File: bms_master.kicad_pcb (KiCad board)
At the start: 4 copper layers, 100 x 50 mm, 25 parts, among them J1 0430450200, J3 TFM-115-02-S-D-WT, J4 0436500200, J4 TFM-115-02-S-D-WT, U2 SM91502ALA-E, U3 SM91502ALA-E

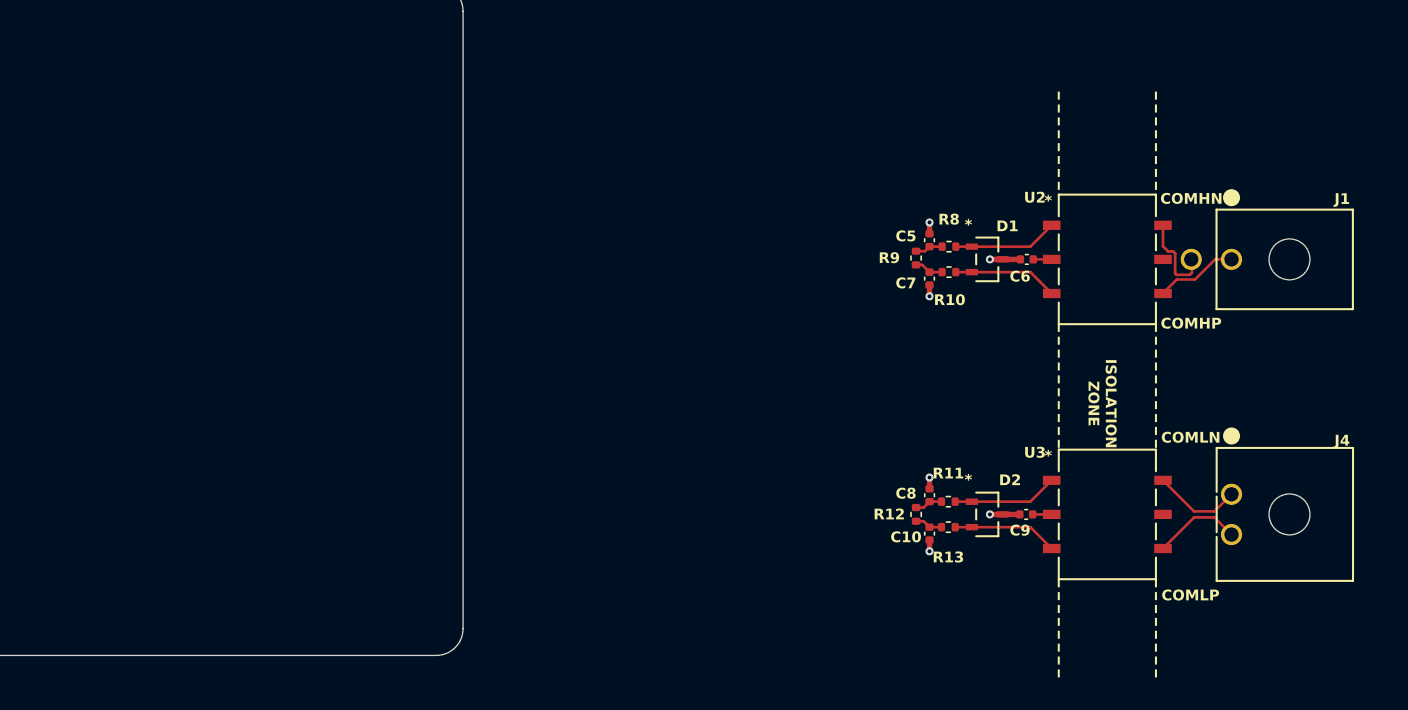
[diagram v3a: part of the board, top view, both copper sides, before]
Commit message: PCB[Fixed Lib Link]: Placed iso parts need to fix arrangment.
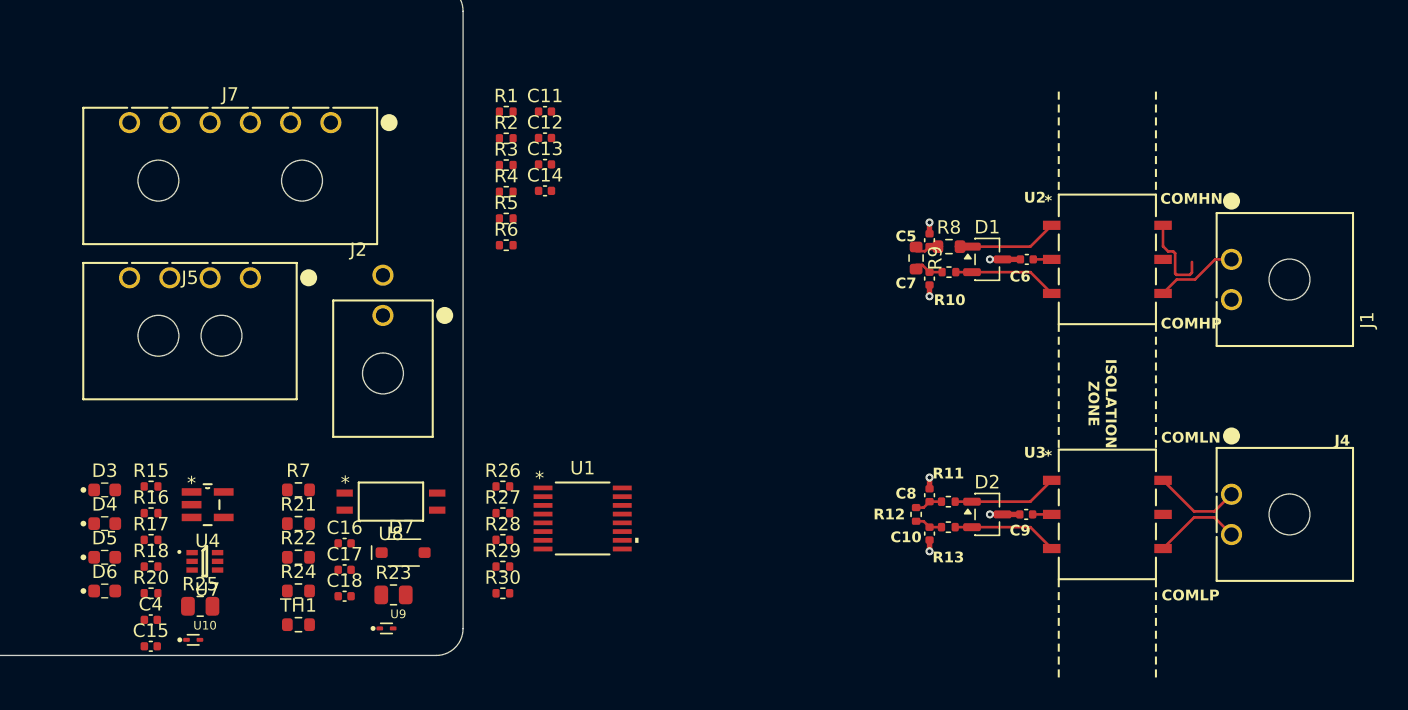
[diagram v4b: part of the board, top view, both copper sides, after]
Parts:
- added C11: 100 pF, remote_cl05a105ko5nnnc:C_0402_1005Metric, F.Cu at (170.1, 65.5)
- added C12: 100 pF, remote_cl05a105ko5nnnc:C_0402_1005Metric, F.Cu at (170.1, 67.5)
- added C13: 100 pF, remote_cl05a105ko5nnnc:C_0402_1005Metric, F.Cu at (170.1, 69.4)
- added C14: 100 pF, remote_cl05a105ko5nnnc:C_0402_1005Metric, F.Cu at (170.1, 71.4)
- added C15: 0.1 µF, remote_cl05a105ko5nnnc:C_0402_1005Metric, F.Cu at (140.7, 105.3)
- added C16: 0.1 µF, remote_cl05a105ko5nnnc:C_0402_1005Metric, F.Cu at (155.2, 97.7)
- added C17: 10 nF, remote_cl05a105ko5nnnc:C_0402_1005Metric, F.Cu at (155.2, 99.6)
- added C18: 10 nF, remote_cl05a105ko5nnnc:C_0402_1005Metric, F.Cu at (155.2, 101.6)
- added C4: 0.1 µF, remote_cl05a105ko5nnnc:C_0402_1005Metric, F.Cu at (140.7, 103.4)
- added D3: Green, remote_ltst-c190tbkt:LED_0603_1608Metric, F.Cu at (137.3, 93.7)
- added D4: Green, remote_ltst-c190tbkt:LED_0603_1608Metric, F.Cu at (137.3, 96.2)
- added D5: RED, remote_ltst-c190tbkt:LED_0603_1608Metric, F.Cu at (137.3, 98.7)
- added D6: RED, remote_ltst-c190tbkt:LED_0603_1608Metric, F.Cu at (137.3, 101.2)
- added D7: 1N4148W, remote_1n4148w:P35_SOD-123F, F.Cu at (157.9, 98.3)
- added J2: 0430450200, remote_0430450200:CONN_SD-43045-001_02_MOL, F.Cu at (158.0, 80.7)
- added J5: 0436500400, remote_0436500400:CONN_SD-43650-001_04_MOL, F.Cu at (148.2, 77.9)
- added J7: 0436500600, remote_0436500600:CONN_SD-43650-001_06_MOL, F.Cu at (154.2, 66.3)
- added R1: 1k, remote_erj-2ge0r00x:R_0402_1005Metric, F.Cu at (167.2, 65.5)
- added R15: 10k, remote_erj-2ge0r00x:R_0402_1005Metric, F.Cu at (140.8, 93.4)
- added R16: 10k, remote_erj-2ge0r00x:R_0402_1005Metric, F.Cu at (140.8, 95.4)
- added R17: 10k, remote_erj-2ge0r00x:R_0402_1005Metric, F.Cu at (140.8, 97.4)
- added R18: 1k, remote_erj-2ge0r00x:R_0402_1005Metric, F.Cu at (140.8, 99.4)
- added R2: 1k, remote_erj-2ge0r00x:R_0402_1005Metric, F.Cu at (167.2, 67.5)
- added R20: 1k, remote_erj-2ge0r00x:R_0402_1005Metric, F.Cu at (140.8, 101.4)
- added R21: 10k, remote_rcs060359r0fkea:R_0603_1608Metric, F.Cu at (151.7, 96.2)
- added R22: 10k, remote_rcs060359r0fkea:R_0603_1608Metric, F.Cu at (151.7, 98.7)
- added R23: 10k, remote_crcw080510k0fkea:R_0805_2012Metric, F.Cu at (158.8, 101.5)
- added R24: 22k, remote_rcs060359r0fkea:R_0603_1608Metric, F.Cu at (151.7, 101.2)
- added R25: 330, remote_crcw080510k0fkea:R_0805_2012Metric, F.Cu at (144.4, 102.3)
- added R26: 10k, remote_erj-2ge0r00x:R_0402_1005Metric, F.Cu at (167.0, 93.4)
- added R27: 10k, remote_erj-2ge0r00x:R_0402_1005Metric, F.Cu at (167.0, 95.4)
- added R28: 10k, remote_erj-2ge0r00x:R_0402_1005Metric, F.Cu at (167.0, 97.4)
- added R29: 10k, remote_erj-2ge0r00x:R_0402_1005Metric, F.Cu at (167.0, 99.4)
- added R3: 49.9, remote_erj-2ge0r00x:R_0402_1005Metric, F.Cu at (167.2, 69.5)
- added R30: 10k, remote_erj-2ge0r00x:R_0402_1005Metric, F.Cu at (167.0, 101.4)
- added R4: 49.9, remote_erj-2ge0r00x:R_0402_1005Metric, F.Cu at (167.2, 71.5)
- added R5: 49.9, remote_erj-2ge0r00x:R_0402_1005Metric, F.Cu at (167.2, 73.5)
- added R6: 49.9, remote_erj-2ge0r00x:R_0402_1005Metric, F.Cu at (167.2, 75.4)
- added R7: 10k, remote_rcs060359r0fkea:R_0603_1608Metric, F.Cu at (151.7, 93.7)
- added TH1: NCP18XH103F03RB, remote_rcs060359r0fkea:R_0603_1608Metric, F.Cu at (151.7, 103.7)
- added U1: BQ79600PWRQ1, remote_bq79600pwrq1:SOIC_9600PWQ1_TEX, F.Cu at (172.9, 95.8)
- added U10: ESD9B5.0ST5G, remote_esd9b3.3st5g:SODFL1006X40N, F.Cu at (143.9, 104.8)
- added U4: SN74LVC1G08QDBVRQ1, remote_sn74lvc1g08qdbvrq1:DBV5, F.Cu at (145.0, 94.8)
- added U7: SN74LVC2G04DCKR, remote_sn74lvc2g04dckr:DCK0006A_N, F.Cu at (144.8, 99.0)
- added U8: TLP293(GB-TPL,E, remote_tlp293_gb-tpl_e:SO4_TOS, F.Cu at (158.6, 94.5)
- added U9: ESD9B5.0ST5G, remote_esd9b3.3st5g:SODFL1006X40N, F.Cu at (158.3, 104.0)
- C10, C8: value 100 pF -> 0.1 µF
- C5: value 100 pF -> 100pF
- C7: value 100 pF -> 220 nF
- C9: value 100pF -> 220 nF
- D1, D2: footprint remote_pesd1can_215:SOT23_PESD1_NEX -> remote_pesd5v0u2bt-qr:SOT-23-3
- J1: value 0430450200 -> 0436500200; footprint remote_0430450200:CONN_SD-43045-001_02_MOL -> remote_0436500200:CONN_SD-43650-001_02_MOL
- R10, R11: value 49.9 -> 1k
- R8: value 49.9 -> 10; footprint remote_erj-2ge0r00x:R_0402_1005Metric -> remote_rcs060359r0fkea:R_0603_1608Metric
- R9: value 1k -> 100k; footprint remote_erj-2ge0r00x:R_0402_1005Metric -> remote_rcs060359r0fkea:R_0603_1608Metric
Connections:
- C10 pad 1: /Project Architecture/GND -> /Project Architecture/Com. Chip/BAT
- C10 pad 2: /Project Architecture/Com. Chip/U1_COML.P -> /Project Architecture/GND
- C5 pad 1: /Project Architecture/GND -> /Project Architecture/Daisy Chain/COMH_CT
- C5 pad 2: /Project Architecture/Com. Chip/U1_COMH.P -> /Project Architecture/GND
- C6 pad 1: /Project Architecture/Daisy Chain/COMH_CT -> /Project Architecture/Daisy Chain/COML_CT
- C7 pad 2: /Project Architecture/Com. Chip/U1_COMH.N -> /Project Architecture/Com. Chip/DVDD
- C8 pad 1: /Project Architecture/GND -> /Project Architecture/+3V3
- C8 pad 2: /Project Architecture/Com. Chip/U1_COML.N -> /Project Architecture/GND
- C9 pad 1: /Project Architecture/Daisy Chain/COML_CT -> /Project Architecture/Com. Chip/CVDD
- J1 pad 1: /Project Architecture/Connectors/COMH.N -> /Project Architecture/Connectors/COML.N
- J1 pad 2: /Project Architecture/Connectors/COMH.P -> /Project Architecture/Connectors/COML.P
- J3 pad 01: /Project Architecture/Connectors/BOARD_TEMP -> /Project Architecture/+12V
- J3 pad 02: /Project Architecture/Connectors/BOARD_TEMP -> /Project Architecture/+12V
- J3 pad 03: /Project Architecture/GND -> /Project Architecture/+5V
- J3 pad 04: /Project Architecture/GND -> /Project Architecture/+5V
- J3 pad 05: unconnected-(J3-ADC1_IN2-Pad05) -> /Project Architecture/+3V3
- J3 pad 06: unconnected-(J3-ADC1_IN2-Pad06) -> /Project Architecture/+3V3
- J3 pad 11: /Project Architecture/GND -> unconnected-(J3-TIM1_CH3-Pad11)
- J3 pad 12: /Project Architecture/GND -> unconnected-(J3-TIM2_CH1-Pad12)
- J3 pad 14: unconnected-(J3-ADC1_IN4-Pad14) -> /Project Architecture/Com. Chip/SPI.nCS
- J3 pad 15: /Project Architecture/GND -> /Project Architecture/Com. Chip/SPI.RDY
- J3 pad 16: /Project Architecture/GND -> /Project Architecture/BMS_OK & Indicators/FB.NFAULT
- J3 pad 17: unconnected-(J3-ADC2_IN5-Pad17) -> /Project Architecture/Connectors/MCU_BMS_OK
- J3 pad 18: unconnected-(J3-ADC2_IN5-Pad18) -> /Project Architecture/Connectors/CHG_MODE_N
- J3 pad 19: /Project Architecture/GND -> /Project Architecture/BMS_OK & Indicators/FB.BMS_OK
- J3 pad 20: /Project Architecture/GND -> /Project Architecture/Connectors/SDC_OK_N
- J3 pad 21: unconnected-(J3-DAC1_OUT2-Pad21) -> /Project Architecture/Com. Chip/SPI.MOSI
- J3 pad 22: unconnected-(J3-DAC1_OUT2-Pad22) -> /Project Architecture/Com. Chip/SPI.MISO
- J3 pad 25: unconnected-(J3-DAC1_OUT1-Pad25) -> /Project Architecture/GND
- J3 pad 26: unconnected-(J3-DAC1_OUT1-Pad26) -> /Project Architecture/Com. Chip/SPI.SCLK
- J3 pad 29: /Project Architecture/GND -> unconnected-(J3-I2C1_SCL-Pad29)
- J3 pad 30: /Project Architecture/GND -> unconnected-(J3-I2C1_SDA-Pad30)
- R10 pad 1: /Project Architecture/Com. Chip/U1_COMH.N -> Net-(D3-A)
- R10 pad 2: /Project Architecture/Daisy Chain/COMH_WN -> /Project Architecture/+3V3
- R11 pad 1: /Project Architecture/Com. Chip/U1_COML.N -> Net-(D4-A)
- R11 pad 2: /Project Architecture/Daisy Chain/COML_WN -> /Project Architecture/BMS_OK & Indicators/BMS_OK_LOGIC
- R8 pad 1: /Project Architecture/Com. Chip/U1_COMH.P -> /Project Architecture/Com. Chip/BAT
- R8 pad 2: /Project Architecture/Daisy Chain/COMH_WP -> /Project Architecture/+12V
- R9 pad 1: /Project Architecture/Com. Chip/U1_COMH.P -> /Project Architecture/BMS_OK & Indicators/NFAULT
- R9 pad 2: /Project Architecture/Com. Chip/U1_COMH.N -> /Project Architecture/+3V3
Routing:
- net (no net): track 8.39 -> 0.00 mm
- net /Project Architecture/GND: track 4.49 -> 9.18 mm, vias 2 -> 5
- net /Project Architecture/Daisy Chain/COMH_CT: track 1.37 -> 3.45 mm
- net /Project Architecture/Com. Chip/U1_COML.P: track 0.84 -> 2.07 mm, vias 1 -> 0
- net /Project Architecture/Com. Chip/U1_COML.N: track 0.84 -> 2.07 mm, vias 1 -> 0
- net /Project Architecture/Com. Chip/U1_COMH.P: track 0.84 -> 0.00 mm, vias 1 -> 0
- net /Project Architecture/Com. Chip/U1_COMH.N: track 0.84 -> 0.00 mm, vias 1 -> 0
- net /Project Architecture/Com. Chip/DVDD: track 0.00 -> 0.84 mm, vias 0 -> 1

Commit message: PCB[Layout, Mounting]:Inital layout and edgecut/hole placment.
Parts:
- removed C16: 0.1 µF, remote_cl05a105ko5nnnc:C_0402_1005Metric
- removed C17, C18: 10 nF, remote_cl05a105ko5nnnc:C_0402_1005Metric
- removed the J4 at (221.2, 94.0)
- removed J7: 0436500600, remote_0436500600:CONN_SD-43650-001_06_MOL
- removed R27, R28, R29, R30: 10k, remote_erj-2ge0r00x:R_0402_1005Metric
- removed U10, U9: ESD9B5.0ST5G, remote_esd9b3.3st5g:SODFL1006X40N
- added C1: 220 nF, remote_cl05a105ko5nnnc:C_0402_1005Metric, F.Cu at (111.5, 77.6)
- added C2: 0.1 µF, remote_cl05a105ko5nnnc:C_0402_1005Metric, F.Cu at (116.6, 77.6)
- added C3: 0.1 µF, remote_cl05a105ko5nnnc:C_0402_1005Metric, F.Cu at (108.4, 79.6)
- added G1: SAE Electric logo, remote_sae_electric_logo:SAE_Electric_Logo_10mm, F.Cu at (73.2, 64.8)
- added G2: BMD Logo, remote_bmd_logo:BDM_Logo_100mm, B.Cu at (116.2, 82.0)
- added R14: 1k, remote_erj-2ge0r00x:R_0402_1005Metric, F.Cu at (79.7, 100.6)
- added R19: 10k, remote_erj-2ge0r00x:R_0402_1005Metric, F.Cu at (105.8, 77.7)
- added U5: ESD9B5.0ST5G, remote_esd9b3.3st5g:SODFL1006X40N, F.Cu at (75.8, 88.0)
- added U6: SN74LVC2G04DCKR, remote_sn74lvc2g04dckr:DCK0006A_N, F.Cu at (77.0, 96.2)
- C10, C8: value 0.1 µF -> 100 pF
- C11, C12: value 100 pF -> 0.1 µF
- C13, C14: value 100 pF -> 10 nF
- C4: value 0.1 µF -> 220 nF
- C5: value 100pF -> 100 pF
- C7: value 220 nF -> 100 pF
- C9: value 220 nF -> 100pF
- J1: value 0436500200 -> 0430450200; footprint remote_0436500200:CONN_SD-43650-001_02_MOL -> remote_0430450200:CONN_SD-43045-001_02_MOL
- J2: value 0430450200 -> 0436500200; footprint remote_0430450200:CONN_SD-43045-001_02_MOL -> remote_0436500200:CONN_SD-43650-001_02_MOL
- J5: value 0436500400 -> 0436500600; footprint remote_0436500400:CONN_SD-43650-001_04_MOL -> remote_0436500600:CONN_SD-43650-001_06_MOL
- R1: value 1k -> 10; footprint remote_erj-2ge0r00x:R_0402_1005Metric -> remote_rcs060359r0fkea:R_0603_1608Metric
- R10, R11: value 1k -> 49.9
- R15: value 10k -> 330; footprint remote_erj-2ge0r00x:R_0402_1005Metric -> remote_crcw080510k0fkea:R_0805_2012Metric
- R16: value 10k -> 1k
- R18: value 1k -> 10k
- R2: value 1k -> 100k; footprint remote_erj-2ge0r00x:R_0402_1005Metric -> remote_rcs060359r0fkea:R_0603_1608Metric
- R21: value 10k -> 1k; footprint remote_rcs060359r0fkea:R_0603_1608Metric -> remote_erj-2ge0r00x:R_0402_1005Metric
- R22: value 10k -> 22k
- R24: value 22k -> 10k
- R25: value 330 -> 10k; footprint remote_crcw080510k0fkea:R_0805_2012Metric -> remote_rcs060359r0fkea:R_0603_1608Metric
- R26: footprint remote_erj-2ge0r00x:R_0402_1005Metric -> remote_rcs060359r0fkea:R_0603_1608Metric
- R3, R4, R5, R6: value 49.9 -> 10k
- R7: footprint remote_rcs060359r0fkea:R_0603_1608Metric -> remote_erj-2ge0r00x:R_0402_1005Metric
- R8: value 10 -> 49.9; footprint remote_rcs060359r0fkea:R_0603_1608Metric -> remote_erj-2ge0r00x:R_0402_1005Metric
- R9: value 100k -> 1k; footprint remote_rcs060359r0fkea:R_0603_1608Metric -> remote_erj-2ge0r00x:R_0402_1005Metric
- U7: value SN74LVC2G04DCKR -> TLP293(GB-TPL,E; footprint remote_sn74lvc2g04dckr:DCK0006A_N -> remote_tlp293_gb-tpl_e:SO4_TOS
- U8: value TLP293(GB-TPL,E -> ESD9B5.0ST5G; footprint remote_tlp293_gb-tpl_e:SO4_TOS -> remote_esd9b3.3st5g:SODFL1006X40N
- moved H2 182.2 mm to (161.0, 103.0)
- moved H3 169.2 mm to (161.0, 81.0)
- moved H4 160.7 mm to (161.0, 59.0)
- moved H1 118.1 mm to (67.0, 103.0)
- moved C12 95.0 mm to (79.6, 96.2), turned to 180 degrees
- moved C11 94.3 mm to (79.2, 90.9), turned to -90 degrees
- moved C14 91.1 mm to (79.8, 83.0), turned to -90 degrees
- moved R23 86.5 mm to (77.0, 73.5)
- moved U8 83.9 mm to (75.8, 81.5), turned to 90 degrees
- moved D7 81.9 mm to (79.9, 73.5), turned to -90 degrees
- moved C13 79.9 mm to (90.4, 74.9), turned to -90 degrees
- moved R24 76.7 mm to (77.8, 81.0)
- moved J5 74.9 mm to (74.0, 88.5), turned to -90 degrees
- moved R25 69.6 mm to (77.8, 82.5)
- moved R21 68.9 mm to (82.8, 97.4), turned to 180 degrees
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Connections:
- C10 pad 1: /Project Architecture/Com. Chip/BAT -> /Project Architecture/GND
- C10 pad 2: /Project Architecture/GND -> /Project Architecture/Com. Chip/U1_COML.P
- C11 pad 1: /Project Architecture/GND -> /Project Architecture/+3V3
- C11 pad 2: /Project Architecture/Com. Chip/U1_COMH.N -> /Project Architecture/GND
- C12 pad 2: /Project Architecture/Com. Chip/U1_COML.P -> /Project Architecture/+3V3
- C13 pad 1: /Project Architecture/GND -> /Project Architecture/Connectors/SDC_OK_N
- C13 pad 2: /Project Architecture/Com. Chip/U1_COMH.P -> /Project Architecture/GND
- C14 pad 1: /Project Architecture/GND -> /Project Architecture/Connectors/CHG_MODE_N
- C14 pad 2: /Project Architecture/Com. Chip/U1_COML.N -> /Project Architecture/GND
- C15 pad 2: /Project Architecture/+3V3 -> /Project Architecture/Connectors/BOARD_TEMP
- C4 pad 1: /Project Architecture/+3V3 -> /Project Architecture/Com. Chip/CVDD
- C5 pad 1: /Project Architecture/Daisy Chain/COMH_CT -> /Project Architecture/GND
- C5 pad 2: /Project Architecture/GND -> /Project Architecture/Com. Chip/U1_COMH.P
- C6 pad 1: /Project Architecture/Daisy Chain/COML_CT -> /Project Architecture/Daisy Chain/COMH_CT
- C7 pad 2: /Project Architecture/Com. Chip/DVDD -> /Project Architecture/Com. Chip/U1_COMH.N
- C8 pad 1: /Project Architecture/+3V3 -> /Project Architecture/GND
- C8 pad 2: /Project Architecture/GND -> /Project Architecture/Com. Chip/U1_COML.N
- C9 pad 1: /Project Architecture/Com. Chip/CVDD -> /Project Architecture/Daisy Chain/COML_CT
- J1 pad 1: /Project Architecture/Connectors/COML.N -> /Project Architecture/Connectors/COMH.N
- J1 pad 2: /Project Architecture/Connectors/COML.P -> /Project Architecture/Connectors/COMH.P
- J2 pad 1: /Project Architecture/Connectors/COMH.N -> /Project Architecture/Connectors/COML.N
- J2 pad 2: /Project Architecture/Connectors/COMH.P -> /Project Architecture/Connectors/COML.P
- J5 pad 1: unconnected-(J5-Pad1) -> /Project Architecture/BMS_OK & Indicators/BMS_OK
- J5 pad 2: unconnected-(J5-Pad2) -> /Project Architecture/GND
- J5 pad 3: unconnected-(J5-Pad3) -> /Project Architecture/Connectors/CHG_MODE
- J5 pad 4: unconnected-(J5-Pad4) -> /Project Architecture/GND
- R1 pad 1: /Project Architecture/Com. Chip/U1_COMH.P -> /Project Architecture/Com. Chip/BAT
- R1 pad 2: /Project Architecture/Com. Chip/U1_COMH.N -> /Project Architecture/+12V
- R10 pad 1: Net-(D3-A) -> /Project Architecture/Com. Chip/U1_COMH.N
- R10 pad 2: /Project Architecture/+3V3 -> /Project Architecture/Daisy Chain/COMH_WN
- R11 pad 1: Net-(D4-A) -> /Project Architecture/Com. Chip/U1_COML.N
- R11 pad 2: /Project Architecture/BMS_OK & Indicators/BMS_OK_LOGIC -> /Project Architecture/Daisy Chain/COML_WN
- R15 pad 1: /Project Architecture/Connectors/MCU_BMS_OK -> /Project Architecture/BMS_OK & Indicators/BMS_OK_LOGIC
- R15 pad 2: /Project Architecture/GND -> /Project Architecture/BMS_OK & Indicators/BMS_OK
- R16 pad 1: /Project Architecture/BMS_OK & Indicators/BMS_OK_LOGIC -> Net-(D4-A)
- R16 pad 2: /Project Architecture/BMS_OK & Indicators/FB.BMS_OK -> /Project Architecture/BMS_OK & Indicators/BMS_OK_LOGIC
- R17 pad 1: /Project Architecture/BMS_OK & Indicators/NFAULT -> /Project Architecture/Connectors/MCU_BMS_OK
- R17 pad 2: /Project Architecture/BMS_OK & Indicators/FB.NFAULT -> /Project Architecture/GND
- R18 pad 1: /Project Architecture/GND -> /Project Architecture/BMS_OK & Indicators/BMS_OK_LOGIC
- R18 pad 2: Net-(D5-K) -> /Project Architecture/BMS_OK & Indicators/FB.BMS_OK
- R2 pad 1: /Project Architecture/Com. Chip/U1_COML.N -> /Project Architecture/BMS_OK & Indicators/NFAULT
- R2 pad 2: /Project Architecture/Com. Chip/U1_COML.P -> /Project Architecture/+3V3
- R20 pad 2: Net-(D6-K) -> Net-(D5-K)
- R21 pad 1: /Project Architecture/Connectors/CHG_MODE -> /Project Architecture/GND
- R21 pad 2: /Project Architecture/Inputs & Sensing/+3V3 -> Net-(D6-K)
- R22 pad 1: /Project Architecture/Connectors/CHG_MODE -> /Project Architecture/Connectors/SDC_OK_N
- R22 pad 2: /Project Architecture/Connectors/CHG_MODE_N -> /Project Architecture/+3V3
- R24 pad 1: /Project Architecture/Connectors/SDC_OK_N -> /Project Architecture/Connectors/CHG_MODE
- R24 pad 2: /Project Architecture/Inputs & Sensing/+3V3 -> /Project Architecture/+3V3
- R25 pad 1: /Project Architecture/BMS_OK & Indicators/BMS_OK_LOGIC -> /Project Architecture/Connectors/CHG_MODE
- R25 pad 2: /Project Architecture/BMS_OK & Indicators/BMS_OK -> /Project Architecture/Connectors/CHG_MODE_N
- R26 pad 2: /Project Architecture/Com. Chip/SPI.SCLK -> /Project Architecture/Connectors/BOARD_TEMP
- R3 pad 1: /Project Architecture/Com. Chip/U1_COMH.P -> /Project Architecture/Com. Chip/SPI.nCS
- R3 pad 2: /Project Architecture/Daisy Chain/COMH_WP -> /Project Architecture/+3V3
- R4 pad 1: /Project Architecture/Com. Chip/U1_COMH.N -> /Project Architecture/Com. Chip/SPI.RDY
- R4 pad 2: /Project Architecture/Daisy Chain/COMH_WN -> /Project Architecture/+3V3
- R5 pad 1: /Project Architecture/Com. Chip/U1_COML.N -> /Project Architecture/Com. Chip/SPI.MOSI
- R5 pad 2: /Project Architecture/Daisy Chain/COML_WN -> /Project Architecture/+3V3
- R6 pad 1: /Project Architecture/Com. Chip/U1_COML.P -> /Project Architecture/Com. Chip/SPI.MISO
- R6 pad 2: /Project Architecture/Daisy Chain/COML_WP -> /Project Architecture/+3V3
- R7 pad 1: /Project Architecture/Inputs & Sensing/GND -> /Project Architecture/GND
- R7 pad 2: /Project Architecture/Connectors/BOARD_TEMP -> /Project Architecture/Com. Chip/SPI.SCLK
- R8 pad 1: /Project Architecture/Com. Chip/BAT -> /Project Architecture/Com. Chip/U1_COMH.P
- R8 pad 2: /Project Architecture/+12V -> /Project Architecture/Daisy Chain/COMH_WP
- R9 pad 1: /Project Architecture/BMS_OK & Indicators/NFAULT -> /Project Architecture/Com. Chip/U1_COMH.P
- R9 pad 2: /Project Architecture/+3V3 -> /Project Architecture/Com. Chip/U1_COMH.N
- TH1 pad 1: /Project Architecture/Inputs & Sensing/+3V3 -> /Project Architecture/+3V3
- U7 pad 1: /Project Architecture/BMS_OK & Indicators/FB.BMS_OK -> Net-(D7-K)
- U7 pad 2: /Project Architecture/GND -> /Project Architecture/Connectors/SDC_SENSE_RTN
- U7 pad 3: /Project Architecture/BMS_OK & Indicators/FB.NFAULT -> /Project Architecture/GND
- U7 pad 4: Net-(D6-A) -> /Project Architecture/Connectors/SDC_OK_N
- U8 pad 1: Net-(D7-K) -> /Project Architecture/Connectors/CHG_MODE
- U8 pad 2: /Project Architecture/Connectors/SDC_SENSE_RTN -> /Project Architecture/GND
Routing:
- net /Project Architecture/Com. Chip/U1_COMH.N: track 0.00 -> 23.9 mm
- net /Project Architecture/Com. Chip/U1_COMH.P: track 0.00 -> 23.8 mm
- net /Project Architecture/Com. Chip/U1_COML.N: track 2.07 -> 21.5 mm
- net /Project Architecture/Com. Chip/U1_COML.P: track 2.07 -> 21.5 mm
- net /Project Architecture/GND: track 9.18 -> 4.58 mm, vias 5 -> 70
- net /Project Architecture/Daisy Chain/COMH_CT: track 3.45 -> 1.37 mm
- net /Project Architecture/Com. Chip/DVDD: track 0.84 -> 0.00 mm, vias 1 -> 0
- added copper zone on B.Cu, net /Project Architecture/GND
- added copper zone on F.Cu, net /Project Architecture/GND
- added copper zone on In1.Cu, net /Project Architecture/GND
- added copper zone on In2.Cu, net /Project Architecture/GND
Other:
- board text added: "${PROJECT_NAME} REVISION: ${REVISION} RELEASE DATE: ${RELEASE_DATE_NUM} DESIGNER: ${DESIGNER}"
- board text added: "FID6"
